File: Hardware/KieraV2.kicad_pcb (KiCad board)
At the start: 2 copper layers, 111 x 63.2 mm, 113 parts, among them J1 Conn_01x04_Male, J2 Conn_01x06_Male, SW1 SW_Rotary2x4, SW10 SW_Push, SW11 SW_MEC_5G, SW2 SW_Rotary2x4, SW3 SW_Push, SW4 SW_Push, SW5 SW_Push, SW6 SW_Push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

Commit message: temporary firmware
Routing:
- net safe5V: track 63.4 -> 64.6 mm
- net GND: vias 280 -> 281
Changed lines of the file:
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@@
   (via (at 147.86 139.69) (size 0.8) (drill 0.4) (layers F.Cu B.Cu) (net 1))
   (via (at 146.41 138.365) (size 0.8) (drill 0.4) (layers F.Cu B.Cu) (net 1))
-  (via (at 147.435 135.29) (size 0.8) (drill 0.4) (layers F.Cu B.Cu) (net 1))
   (via (at 132.6 144.15) (size 0.8) (drill 0.4) (layers F.Cu B.Cu) (net 1))
   (via (at 128.95 144.075) (size 0.8) (drill 0.4) (layers F.Cu B.Cu) (net 1))
@@
   (via (at 142.38 127.91) (size 0.8) (drill 0.4) (layers F.Cu B.Cu) (net 1))
   (via (at 183.57 110.31) (size 0.8) (drill 0.4) (layers F.Cu B.Cu) (net 1))
+  (via (at 146.23 132.81) (size 0.8) (drill 0.4) (layers F.Cu B.Cu) (net 1))
+  (via (at 146.65 123.3) (size 0.8) (drill 0.4) (layers F.Cu B.Cu) (net 1))
   (segment (start 152.525 104.775) (end 152.85 105.1) (width 0.25) (layer F.Cu) (net 2))
   (segment (start 151.05 104.775) (end 152.525 104.775) (width 0.25) (layer F.Cu) (net 2))
@@
   (segment (start 138.585 128.04) (end 138.51 127.965) (width 1) (layer F.Cu) (net 100))
   (segment (start 138.585 130.16) (end 138.585 128.04) (width 1) (layer F.Cu) (net 100))
-  (via (at 145.6 133.42) (size 0.8) (drill 0.4) (layers F.Cu B.Cu) (net 101))
-  (segment (start 144.855 133.42) (end 145.6 133.42) (width 1) (layer F.Cu) (net 101))
-  (segment (start 143.21 131.775) (end 144.855 133.42) (width 1) (layer F.Cu) (net 101))
-  (segment (start 143.21 130.375) (end 143.21 131.775) (width 1) (layer F.Cu) (net 101))
-  (segment (start 174.625 116.8) (end 174.625 114.4) (width 1) (layer B.Cu) (net 101))
-  (segment (start 158.005 133.42) (end 174.625 116.8) (width 1) (layer B.Cu) (net 101))
-  (segment (start 145.6 133.42) (end 158.005 133.42) (width 1) (layer B.Cu) (net 101))
+  (via (at 145.67 134.66) (size 0.8) (drill 0.4) (layers F.Cu B.Cu) (net 101))
+  (segment (start 143.21 132.2) (end 145.67 134.66) (width 1) (layer F.Cu) (net 101))
+  (segment (start 143.21 130.375) (end 143.21 132.2) (width 1) (layer F.Cu) (net 101))
+  (segment (start 174.625 116.8) (end 156.765 134.66) (width 1) (layer B.Cu) (net 101))
+  (segment (start 174.625 114.4) (end 174.625 116.8) (width 1) (layer B.Cu) (net 101))
+  (segment (start 156.765 134.66) (end 145.67 134.66) (width 1) (layer B.Cu) (net 101))
   (zone (net 1) (net_name GND) (layer F.Cu) (hatch edge 0.508)
     (connect_pads (clearance 0.508))

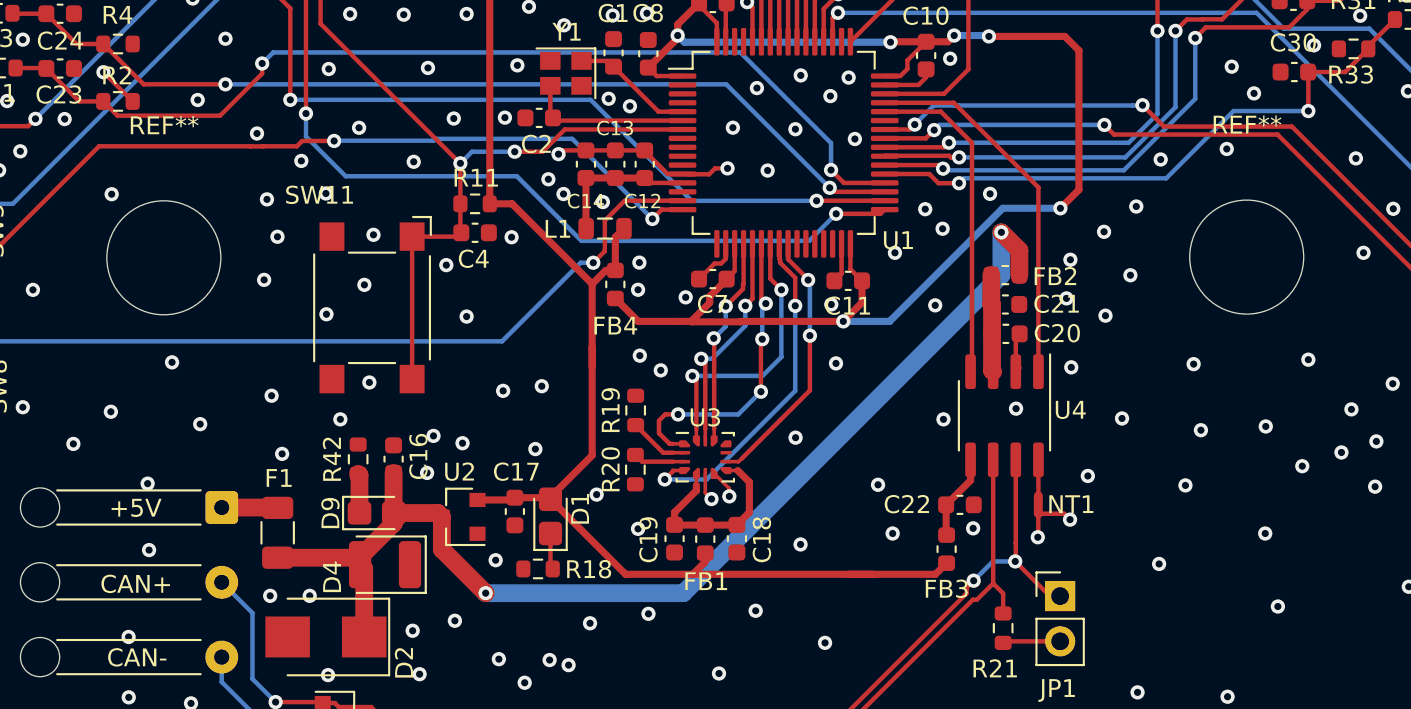
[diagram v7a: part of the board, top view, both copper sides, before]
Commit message: changed uC configuration
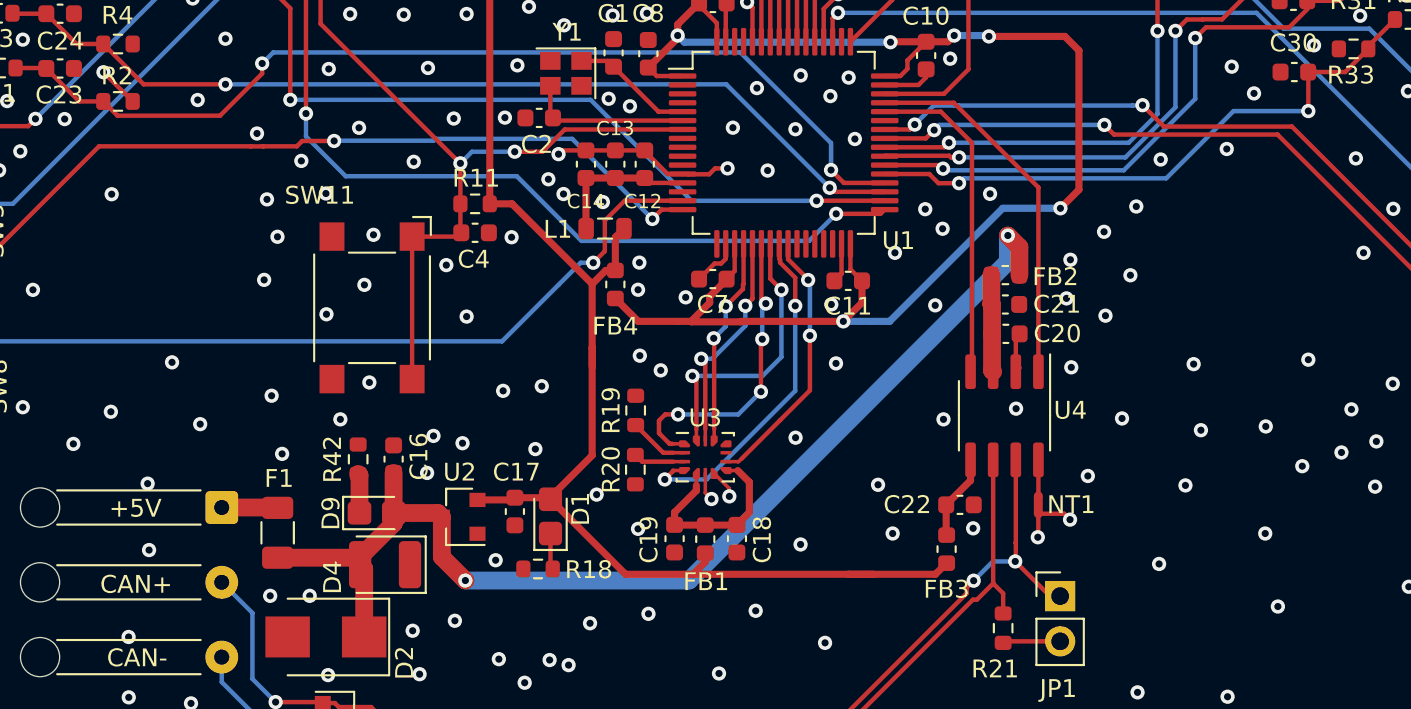
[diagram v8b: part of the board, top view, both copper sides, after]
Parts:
- removed REF** (x2): MountingHole_6.4mm_M6, MountingHole:MountingHole_6.4mm_M6
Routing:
- net safe5V: track 64.6 -> 63.7 mm
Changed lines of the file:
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@@
     (tracks 1002)
     (zones 0)
-    (modules 113)
+    (modules 111)
     (nets 102)
   )
@@
     (34 B.Paste user)
     (35 F.Paste user)
-    (36 B.SilkS user)
-    (37 F.SilkS user)
+    (36 B.SilkS user hide)
+    (37 F.SilkS user hide)
     (38 B.Mask user)
     (39 F.Mask user)
-    (40 Dwgs.User user)
+    (40 Dwgs.User user hide)
     (41 Cmts.User user)
     (42 Eco1.User user)
@@
     (add_net /IMU/+3.3V_IMU)
   )
-  (module MountingHole:MountingHole_6.4mm_M6 (layer F.Cu)
-    (at 127.6 115.83)
-    (descr "Mounting Hole 6.4mm, no annular, M6")
-    (tags "mounting hole 6.4mm no annular m6")
-    (attr virtual)
-    (fp_text reference REF** (at 0 -7.4) (layer F.SilkS)
-      (effects (font (size 1 1) (thickness 0.15)))
-    )
-    (fp_text value MountingHole_6.4mm_M6 (at 0 7.4) (layer F.Fab)
-      (effects (font (size 1 1) (thickness 0.15)))
-    )
-    (fp_text user %R (at 0.3 0) (layer F.Fab)
-      (effects (font (size 1 1) (thickness 0.15)))
-    )
-    (fp_circle (center 0 0) (end 6.4 0) (layer Cmts.User) (width 0.15))
-    (fp_circle (center 0 0) (end 6.65 0) (layer F.CrtYd) (width 0.05))
-    (pad 1 np_thru_hole circle (at 0 0) (size 6.4 6.4) (drill 6.4) (layers *.Cu *.Mask))
-  )
-  (module MountingHole:MountingHole_6.4mm_M6 (layer F.Cu)
-    (at 188.4 115.79)
-    (descr "Mounting Hole 6.4mm, no annular, M6")
-    (tags "mounting hole 6.4mm no annular m6")
-    (attr virtual)
-    (fp_text reference REF** (at 0 -7.4) (layer F.SilkS)
-      (effects (font (size 1 1) (thickness 0.15)))
-    )
-    (fp_text value MountingHole_6.4mm_M6 (at 0 7.4) (layer F.Fab)
-      (effects (font (size 1 1) (thickness 0.15)))
-    )
-    (fp_text user %R (at 0.3 0) (layer F.Fab)
-      (effects (font (size 1 1) (thickness 0.15)))
-    )
-    (fp_circle (center 0 0) (end 6.4 0) (layer Cmts.User) (width 0.15))
-    (fp_circle (center 0 0) (end 6.65 0) (layer F.CrtYd) (width 0.05))
-    (pad 1 np_thru_hole circle (at 0 0) (size 6.4 6.4) (drill 6.4) (layers *.Cu *.Mask))
-  )
   (module Resistor_SMD:R_0603_1608Metric (layer F.Cu)
     (at 138.51 127.14 90)
@@
       (effects (font (size 1 1) (thickness 0.15)))
     )
-    (fp_text user %R (at 0 0 90) (layer F.Fab)
-      (effects (font (size 0.4 0.4) (thickness 0.06)))
-    )
     (fp_line (start -0.8 0.4125) (end -0.8 -0.4125) (layer F.Fab) (width 0.1))
     (fp_line (start -0.8 -0.4125) (end 0.8 -0.4125) (layer F.Fab) (width 0.1))
@@
     (fp_line (start 1.48 -0.73) (end 1.48 0.73) (layer F.CrtYd) (width 0.05))
     (fp_line (start 1.48 0.73) (end -1.48 0.73) (layer F.CrtYd) (width 0.05))
+    (fp_text user %R (at 0 0 90) (layer F.Fab)
+      (effects (font (size 0.4 0.4) (thickness 0.06)))
+    )
     (pad 2 smd roundrect (at 0.825 0 90) (size 0.8 0.95) (layers F.Cu F.Paste F.Mask) (roundrect_rratio 0.25)
       (net 1 GND))
@@
       (effects (font (size 1 1) (thickness 0.15)))
     )
-    (fp_text user %R (at 0 0 90) (layer F.Fab)
-      (effects (font (size 0.8 0.8) (thickness 0.12)))
-    )
     (fp_line (start -1.6 0.8) (end -1.6 -0.8) (layer F.Fab) (width 0.1))
     (fp_line (start -1.6 -0.8) (end 1.6 -0.8) (layer F.Fab) (width 0.1))
@@
     (fp_line (start 2.28 -1.12) (end 2.28 1.12) (layer F.CrtYd) (width 0.05))
     (fp_line (start 2.28 1.12) (end -2.28 1.12) (layer F.CrtYd) (width 0.05))
+    (fp_text user %R (at 0 0 90) (layer F.Fab)
+      (effects (font (size 0.8 0.8) (thickness 0.12)))
+    )
     (pad 2 smd roundrect (at 1.4 0 270) (size 1.25 1.75) (layers F.Cu F.Paste F.Mask) (roundrect_rratio 0.2)
       (net 101 safe5V))
@@
       (effects (font (size 1 1) (thickness 0.15)))
     )
-    (fp_text user %R (at 0 0) (layer F.Fab)
-      (effects (font (size 0.5 0.5) (thickness 0.08)))
-    )
     (fp_line (start 1 -0.6) (end -0.7 -0.6) (layer F.Fab) (width 0.1))
     (fp_line (start -0.7 -0.6) (end -1 -0.3) (layer F.Fab) (width 0.1))
@@
     (fp_line (start 1.88 -0.9) (end 1.88 0.9) (layer F.CrtYd) (width 0.05))
     (fp_line (start 1.88 0.9) (end -1.88 0.9) (layer F.CrtYd) (width 0.05))
+    (fp_text user %R (at 0 0) (layer F.Fab)
+      (effects (font (size 0.5 0.5) (thickness 0.08)))
+    )
     (pad 2 smd roundrect (at 0.9625 0) (size 1.325 1.3) (layers F.Cu F.Paste F.Mask) (roundrect_rratio 0.192308)
       (net 101 safe5V))
@@
       (effects (font (size 1 1) (thickness 0.15)))
     )
-    (fp_text user %R (at 0 0) (layer F.Fab)
-      (effects (font (size 0.8 0.8) (thickness 0.12)))
-    )
     (fp_line (start 1.6 -1.25) (end -0.975 -1.25) (layer F.Fab) (width 0.1))
     (fp_line (start -0.975 -1.25) (end -1.6 -0.625) (layer F.Fab) (width 0.1))
@@
     (fp_line (start 2.28 -1.58) (end 2.28 1.58) (layer F.CrtYd) (width 0.05))
     (fp_line (start 2.28 1.58) (end -2.28 1.58) (layer F.CrtYd) (width 0.05))
+    (fp_text user %R (at 0 0) (layer F.Fab)
+      (effects (font (size 0.8 0.8) (thickness 0.12)))
+    )
     (pad 2 smd roundrect (at 1.4 0 180) (size 1.25 2.65) (layers F.Cu F.Paste F.Mask) (roundrect_rratio 0.2)
       (net 101 safe5V))
@@
   (segment (start 153.5225 133.6) (end 157.3 133.6) (width 0.4) (layer F.Cu) (net 8))
   (segment (start 149.31 129.3875) (end 153.5225 133.6) (width 0.4) (layer F.Cu) (net 8))
-  (via (at 174.625 114.4) (size 0.8) (drill 0.4) (layers F.Cu B.Cu) (net 101))
-  (segment (start 175.6375 115.4125) (end 174.625 114.4) (width 1) (layer F.Cu) (net 101))
-  (segment (start 175.6375 116.8) (end 175.6375 115.4125) (width 1) (layer F.Cu) (net 101))
   (segment (start 133.97 129.85) (end 133.99 129.87) (width 1) (layer F.Cu) (net 9))
   (segment (start 130.85 129.85) (end 133.97 129.85) (width 1) (layer F.Cu) (net 9))
@@
   (segment (start 201.96 121.7) (end 201.13 122.53) (width 0.25) (layer F.Cu) (net 99))
   (segment (start 201.96 119.94) (end 201.96 121.7) (width 0.25) (layer F.Cu) (net 99))
+  (segment (start 138.51 130.085) (end 138.585 130.16) (width 0.25) (layer F.Cu) (net 100))
+  (segment (start 138.585 128.04) (end 138.51 127.965) (width 1) (layer F.Cu) (net 100))
+  (segment (start 138.585 130.16) (end 138.585 128.04) (width 1) (layer F.Cu) (net 100))
   (segment (start 140.51 130.16) (end 140.51 130.24) (width 0.25) (layer F.Cu) (net 101))
   (segment (start 140.5 130.15) (end 140.51 130.16) (width 1) (layer F.Cu) (net 101))
@@
   (segment (start 142.995 130.16) (end 143.21 130.375) (width 1) (layer F.Cu) (net 101))
   (segment (start 140.51 130.16) (end 142.995 130.16) (width 1) (layer F.Cu) (net 101))
-  (segment (start 138.51 130.085) (end 138.585 130.16) (width 0.25) (layer F.Cu) (net 100))
-  (segment (start 138.585 128.04) (end 138.51 127.965) (width 1) (layer F.Cu) (net 100))
-  (segment (start 138.585 130.16) (end 138.585 128.04) (width 1) (layer F.Cu) (net 100))
-  (via (at 145.67 134.66) (size 0.8) (drill 0.4) (layers F.Cu B.Cu) (net 101))
-  (segment (start 143.21 132.2) (end 145.67 134.66) (width 1) (layer F.Cu) (net 101))
-  (segment (start 143.21 130.375) (end 143.21 132.2) (width 1) (layer F.Cu) (net 101))
-  (segment (start 174.625 116.8) (end 156.765 134.66) (width 1) (layer B.Cu) (net 101))
-  (segment (start 174.625 114.4) (end 174.625 116.8) (width 1) (layer B.Cu) (net 101))
-  (segment (start 156.765 134.66) (end 145.67 134.66) (width 1) (layer B.Cu) (net 101))
+  (segment (start 175.6375 115.2275) (end 174.99 114.58) (width 1) (layer F.Cu) (net 101))
+  (via (at 174.99 114.58) (size 0.8) (drill 0.4) (layers F.Cu B.Cu) (net 101))
+  (segment (start 175.6375 116.8) (end 175.6375 115.2275) (width 1) (layer F.Cu) (net 101))
+  (via (at 144.53 133.95) (size 0.8) (drill 0.4) (layers F.Cu B.Cu) (net 101))
+  (segment (start 157.088002 133.95) (end 144.53 133.95) (width 1) (layer B.Cu) (net 101))
+  (segment (start 174.99 116.048002) (end 157.088002 133.95) (width 1) (layer B.Cu) (net 101))
+  (segment (start 174.99 114.58) (end 174.99 116.048002) (width 1) (layer B.Cu) (net 101))
+  (segment (start 143.21 132.63) (end 143.21 130.375) (width 1) (layer F.Cu) (net 101))
+  (segment (start 144.53 133.95) (end 143.21 132.63) (width 1) (layer F.Cu) (net 101))
   (zone (net 1) (net_name GND) (layer F.Cu) (hatch edge 0.508)
     (connect_pads (clearance 0.508))
